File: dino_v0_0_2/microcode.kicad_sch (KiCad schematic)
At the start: 10 parts, among them U15 AT28C64B, U16 74LS244N, U17 74LS244N, U23 AT28C64B, U9 AT28C64B

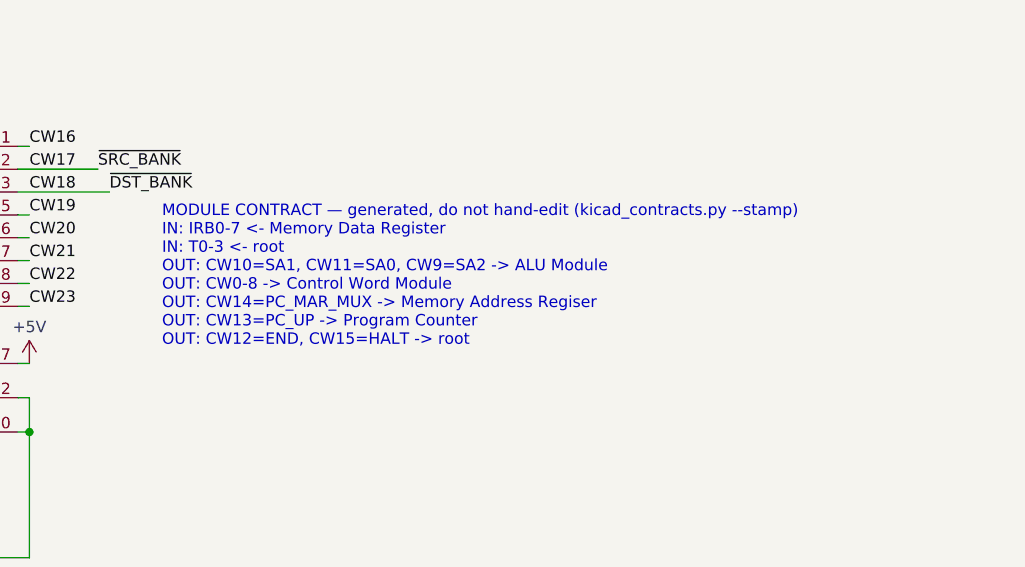
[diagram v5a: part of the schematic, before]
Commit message: feat: phase D on silicon — the machine executes from RAM
PROG_ramexec returns 0x6E. The PC has been above 0x7FFF and FETCH_RAM has
been high, both for the first time in this machine's life.

The missing condition was never "is this a fetch." ~ROM_OUT is asserted for
every src=ROM — opcode fetch, LDAI's immediate, LDA/STA/JMP/CALL operand
bytes — so an instruction living in RAM must read its operands from RAM
too. The condition is "a ROM-side read was requested, but the address is
above 0x7FFF":

    FETCH_RAM = NOR(~ROM_OUT, ~RAM_EN)

Six gate sections, no new IC. All six were free on U22/U37/U39, already in
sockets on the MDR board, where ~ROM_OUT and ~RAM_OUT already sit feeding
READS_IDLE. Only ~RAM_EN had to be brought in.

    U22 g3   FETCH_RAM     = NOR(~ROM_OUT, ~RAM_EN)
    U22 g4   ROM_BUF_ON    = NOR(~ROM_OUT, FETCH_RAM)
    U37 inv4 ~{FETCH_RAM}
    U37 inv6 ~{ROM_BUF_EN} = OR(~ROM_OUT, FETCH_RAM)   -> U19.19
    U37 inv5 ~{RAM_OE_G}   = AND(~RAM_OUT, ~FETCH_RAM) -> U26.22 + U51.9
    U39 g4   RAM_OE_ON     = NAND(~RAM_OUT, ~FETCH_RAM)

Two pin lifts on the memory board, eleven wires. U24.22 stays on ~ROM_OUT:
U24's own ~CE = M15 already deselects the ROM chip at RAM addresses.

Gating ~RAM_OUT upstream is what keeps this at six gates rather than eight.
U51 is a 7400 computing ~RAM_MDR_EN = AND(~RAM_OUT, ~WRITE_DIR), so one
gate on ~RAM_OUT moves both the RAM chip's ~OE and its buffer's ~CE.

Re-proved before building: all 15 src=ROM microcode rows carry mux_pc=True,
FETCH included, and FILL is src=NONE. A ROM-side read can now land in RAM,
so the standing "ROM reads are exempt from the src=RAM -> MAR loop" rule was
no longer free. It holds — MAR never drives M during a ROM-side read, and a
runaway opcode cannot open the loop either.

The witness is not permutation-blind. If the fetch had still come from ROM,
PC=0x9000 presents A0-A14 = 0x1000 to U24, which is 0xFF fill, which is
HALT, so the poison would have survived as 0xFF. 0x6E is 0x8B - 0x1D,
compu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
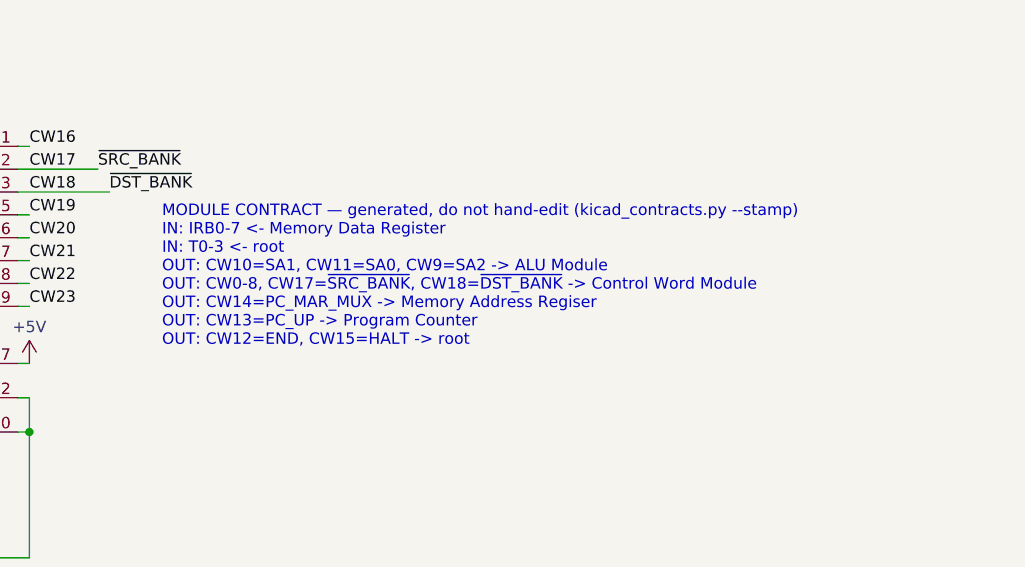
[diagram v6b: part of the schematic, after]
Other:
- note added: "MODULE CONTRACT — generated, do not hand-edit (kicad_contracts.py --stamp) IN: IRB0-7 <- Memory Data Register IN: T0-3 <- root OUT: CW10=SA1, CW11=SA0, CW9=SA2 -> ALU Module OUT: CW0-8, CW17=~{SRC_BANK}, CW18=~{DST_BANK} -> Control Word Module OUT: CW14=PC_MAR_MUX -> Memory Address Regiser OUT: CW13=PC_UP -> Program Counter OUT: CW12=END, CW15=HALT -> root"
- note removed: "MODULE CONTRACT — generated, do not hand-edit (kicad_contracts.py --stamp) IN: IRB0-7 <- Memory Data Register IN: T0-3 <- root OUT: CW10=SA1, CW11=SA0, CW9=SA2 -> ALU Module OUT: CW0-8 -> Control Word Module OUT: CW14=PC_MAR_MUX -> Memory Address Regiser OUT: CW13=PC_UP -> Program Counter OUT: CW12=END, CW15=HALT -> root"
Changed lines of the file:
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@@
 		(comment 4 "A Turing-Complete 8-bit \"Computer\"")
 	)
-	(text "MODULE CONTRACT — generated, do not hand-edit (kicad_contracts.py --stamp)\nIN: IRB0-7 <- Memory Data Register\nIN: T0-3 <- root\nOUT: CW10=SA1, CW11=SA0, CW9=SA2 -> ALU Module\nOUT: CW0-8 -> Control Word Module\nOUT: CW14=PC_MAR_MUX -> Memory Address Regiser\nOUT: CW13=PC_UP -> Program Counter\nOUT: CW12=END, CW15=HALT -> root"
-		(exclude_from_sim no)
-		(at 159.512 170.942 0)
-		(effects
-			(font
-				(size 1.27 1.27)
-			)
-			(justify left bottom)
-		)
-	)
 	(junction
 		(at 53.34 74.93)
@@
 		)
 	)
+	(text "MODULE CONTRACT — generated, do not hand-edit (kicad_contracts.py --stamp)\nIN: IRB0-7 <- Memory Data Register\nIN: T0-3 <- root\nOUT: CW10=SA1, CW11=SA0, CW9=SA2 -> ALU Module\nOUT: CW0-8, CW17=~{SRC_BANK}, CW18=~{DST_BANK} -> Control Word Module\nOUT: CW14=PC_MAR_MUX -> Memory Address Regiser\nOUT: CW13=PC_UP -> Program Counter\nOUT: CW12=END, CW15=HALT -> root"
+		(exclude_from_sim no)
+		(at 159.512 170.942 0)
+		(effects
+			(font
+				(size 1.27 1.27)
+			)
+			(justify left bottom)
+		)
+	)
